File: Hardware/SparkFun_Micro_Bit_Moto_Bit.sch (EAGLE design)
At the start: 47 parts, among them J1 POWER_JACKPTH_LOCK, J2 CORTEX_DEBUGPTH, U1 CY8C4245LQI-483, U2 TPS62172, U3 micro:bit, U4 DRV8835

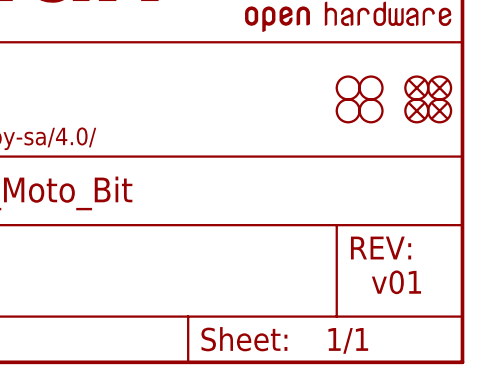
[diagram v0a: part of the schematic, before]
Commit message: V10 Changes
- Replaced 2x3 female headers to male
- Changed net label on heatsink mounting hole to GND
- Increased distance between exposed pad and motor connectors
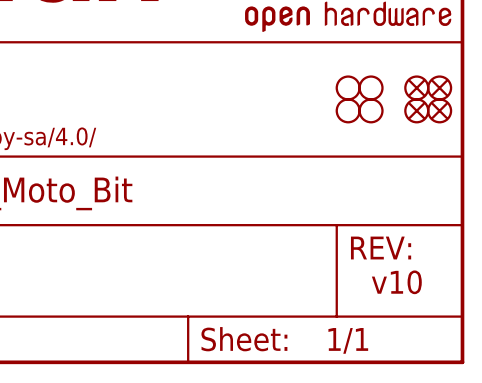
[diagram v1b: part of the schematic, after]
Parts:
- J6, J7, J8, J9: device SparkFun-Connectors:CONN_03X2FEMALE_SMD -> SparkFun-Connectors:CONN_03X2SMT
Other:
- note added: "v10"
- note removed: "v01"
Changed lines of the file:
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@@
 <parts>
 <part name="FRAME1" library="SparkFun-Aesthetics" deviceset="FRAME-LETTER" device=""/>
-<part name="J6" library="SparkFun-Connectors" deviceset="CONN_03X2" device="FEMALE_SMD"/>
-<part name="J7" library="SparkFun-Connectors" deviceset="CONN_03X2" device="FEMALE_SMD"/>
-<part name="J8" library="SparkFun-Connectors" deviceset="CONN_03X2" device="FEMALE_SMD"/>
+<part name="J6" library="SparkFun-Connectors" deviceset="CONN_03X2" device="SMT"/>
+<part name="J7" library="SparkFun-Connectors" deviceset="CONN_03X2" device="SMT"/>
+<part name="J8" library="SparkFun-Connectors" deviceset="CONN_03X2" device="SMT"/>
 <part name="J3" library="SparkFun-Connectors" deviceset="CONN_04" device="SMD_STRAIGHT_COMBO"/>
 <part name="GND22" library="SparkFun-PowerSymbols" deviceset="GND" device=""/>
@@
 <part name="FD3" library="SparkFun-Aesthetics" deviceset="FIDUCIAL" device="UFIDUCIAL"/>
 <part name="FD4" library="SparkFun-Aesthetics" deviceset="FIDUCIAL" device="UFIDUCIAL"/>
-<part name="J9" library="SparkFun-Connectors" deviceset="CONN_03X2" device="FEMALE_SMD"/>
+<part name="J9" library="SparkFun-Connectors" deviceset="CONN_03X2" device="SMT"/>
 <part name="GND26" library="SparkFun-PowerSymbols" deviceset="GND" device=""/>
 <part name="GND30" library="SparkFun-PowerSymbols" deviceset="GND" device=""/>
@@
 <text x="114.3" y="180.34" size="2.54" layer="97">micro:bit</text>
 <text x="166.37" y="11.43" size="2.54" layer="94">Alex Wende</text>
-<text x="238.76" y="7.62" size="2.54" layer="94">v01</text>
+<text x="238.76" y="7.62" size="2.54" layer="94">v10</text>
 <text x="2.54" y="142.24" size="2.54" layer="97">PSoC</text>
 <wire x1="111.76" y1="55.88" x2="111.76" y2="104.14" width="0.2032" layer="97" style="longdash"/>

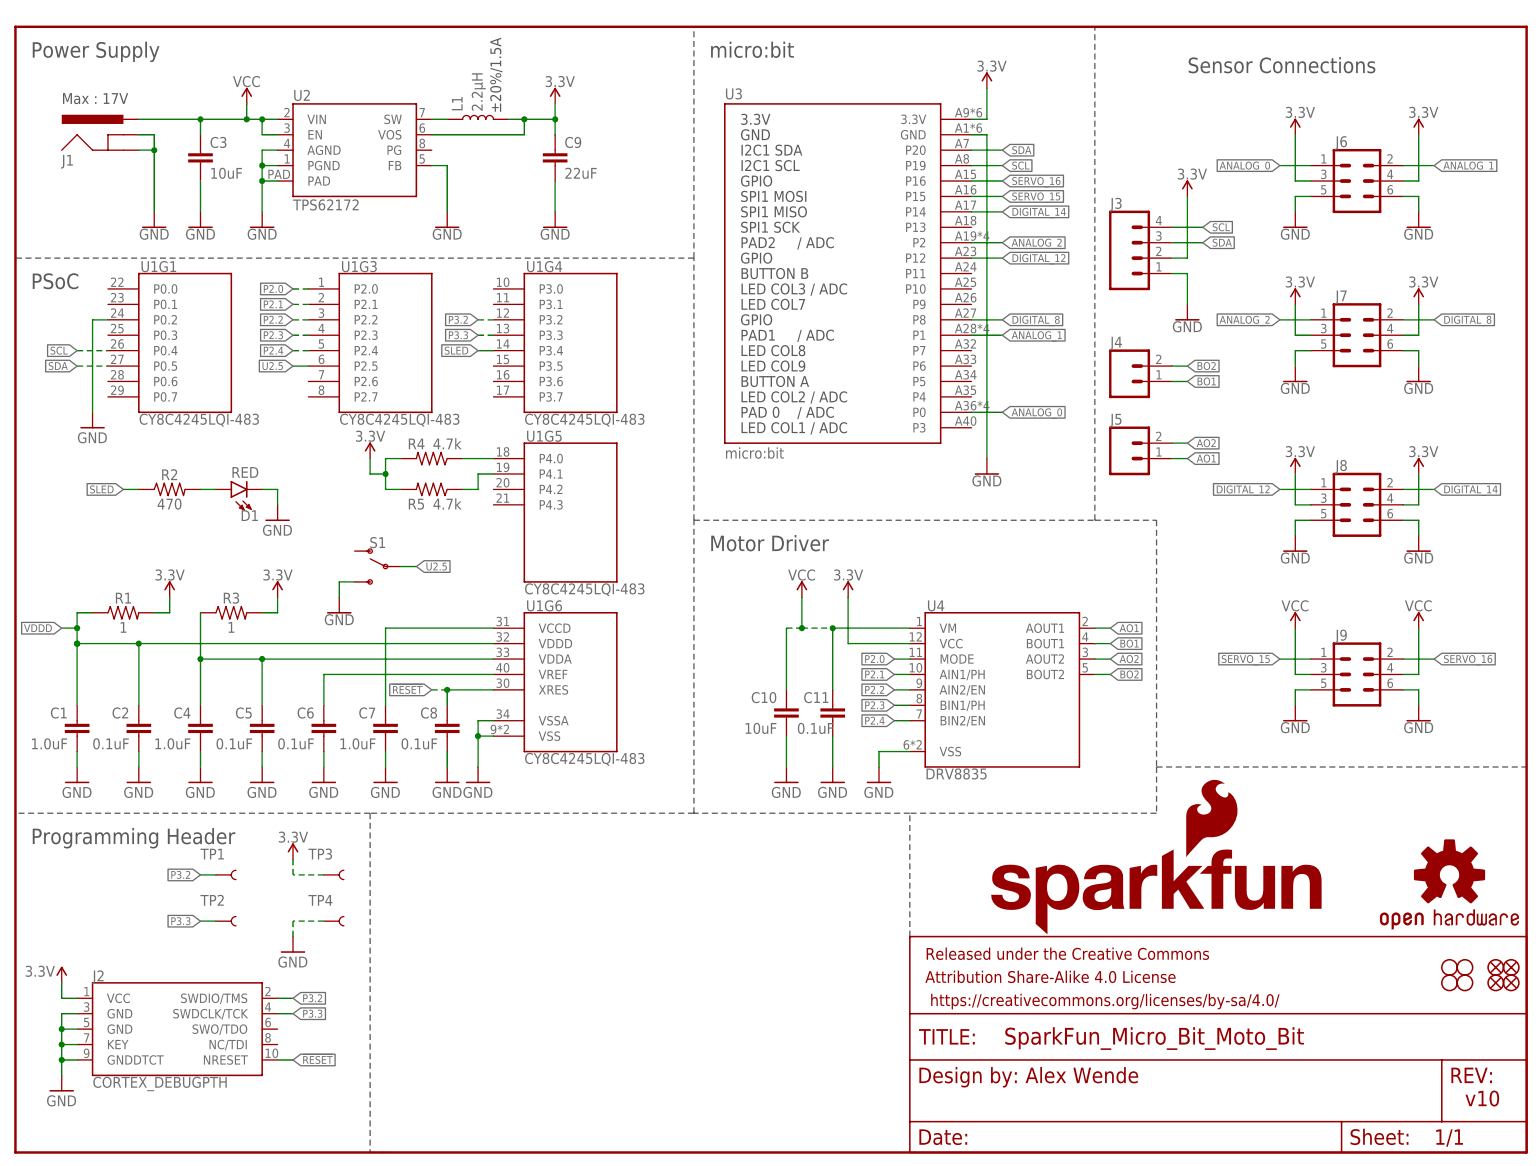
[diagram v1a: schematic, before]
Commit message: v20
-Updated silk to buzzard text
-Updated the supply range to 11V max
-Replaced 2.2uH inductor of buck regulator
-Added QWIIC Connector
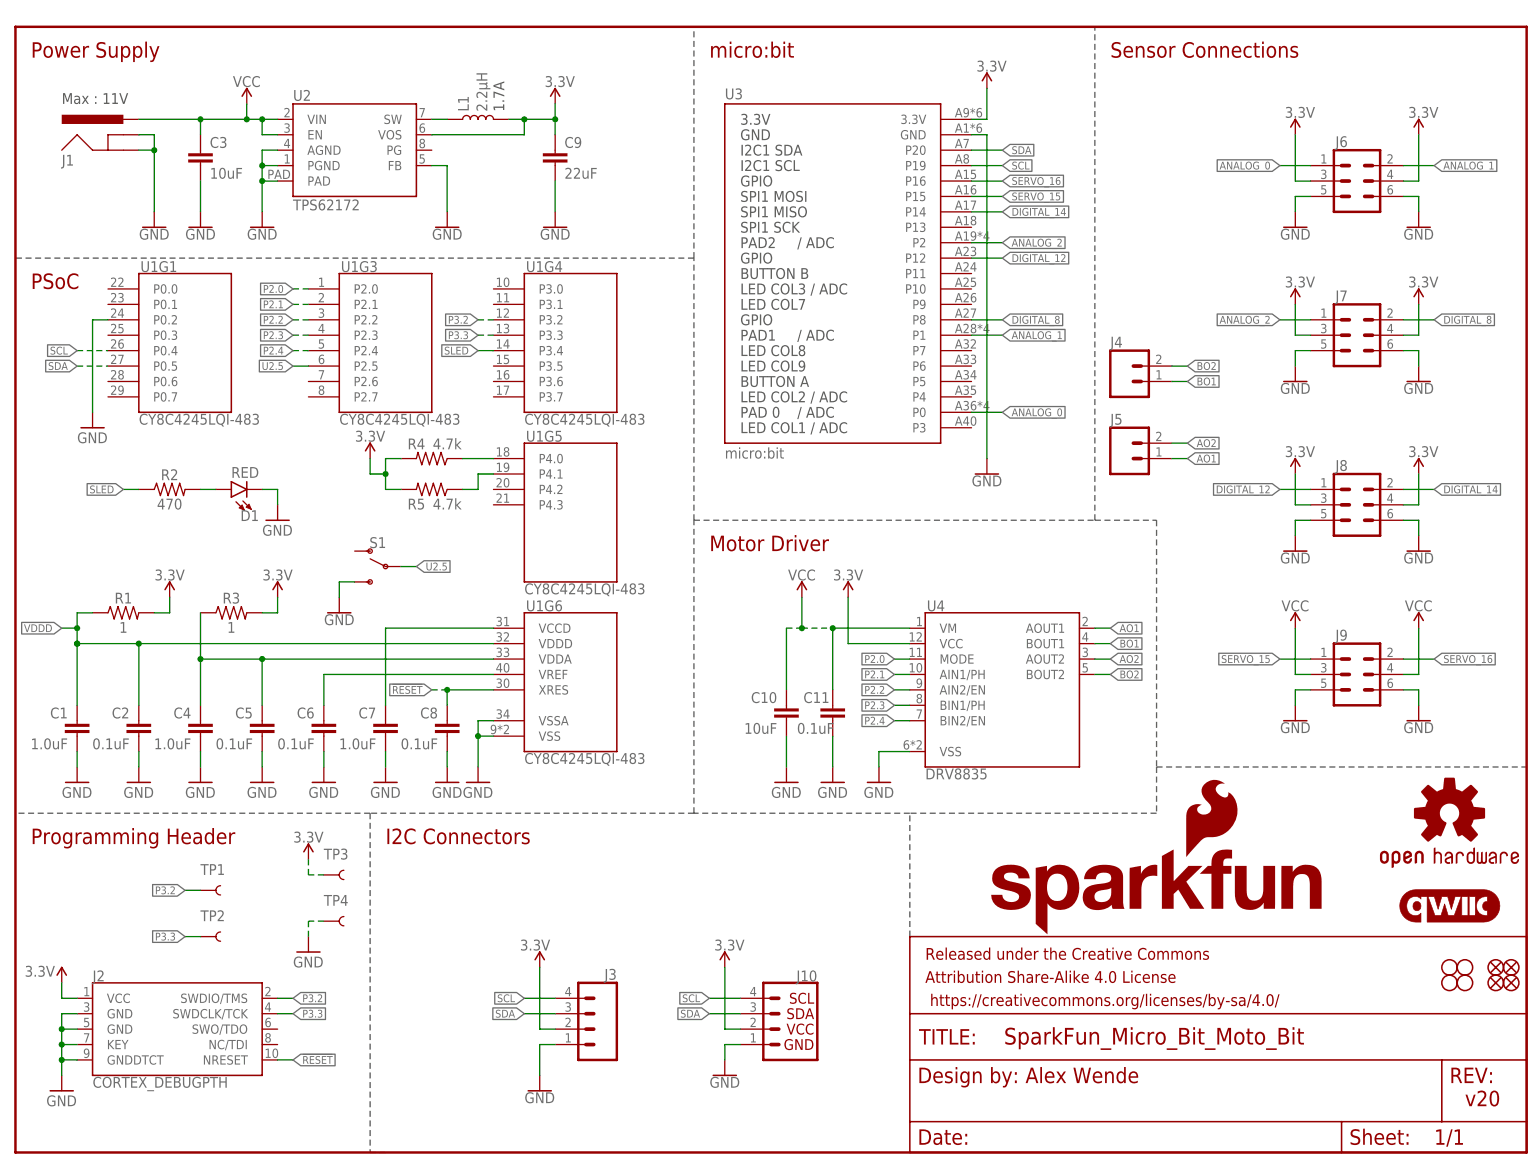
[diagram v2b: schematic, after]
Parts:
- added J10: (no value), SparkFun-Connectors:QWIIC_CONNECTOR
- added LOGO3: QWIIC_LOGO_5MM, SparkFun-Aesthetics:QWIIC_LOGO_5MM
- L1: value 2.2µH -> 2.2μH; device SparkFun-Coils:INDUCTOR-VLF4012AT-2.2UH -> SparkFun-Coils:2.2μH-0805_WIDE-2.2μH-1.7A-0.14OHM
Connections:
- net 3.3V: now also J10.2
- net GND: now also J10.1
- net SCL: now also J10.4
- net SDA: now also J10.3
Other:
- note added: "1.7A"
- note added: "I2C Connectors"
- note added: "Max : 11V"
- note added: "v20"
- note removed: "Max : 17V"
- note removed: "v10"
- note removed: "±20%/1.5A"
- moved on the sheet: J3, TP1, TP2

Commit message: QC Fixes
Replaced switch with short leads
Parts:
- S1: device SparkFun-Switches:SWITCH-SPDT-PTH-11.6X4.0MM -> SparkFun-Switches:SWITCH-SPDT-PTH-11.6X4.0MM-SHORT_LEADS
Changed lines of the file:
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@@
 <part name="SUPPLY3" library="SparkFun-PowerSymbols" deviceset="VCC" device=""/>
 <part name="SUPPLY8" library="SparkFun-PowerSymbols" deviceset="VCC" device=""/>
-<part name="S1" library="SparkFun-Switches" deviceset="SWITCH-SPDT" device="-PTH-11.6X4.0MM"/>
+<part name="S1" library="SparkFun-Switches" deviceset="SWITCH-SPDT" device="-PTH-11.6X4.0MM-SHORT_LEADS"/>
 <part name="GND31" library="SparkFun-Aesthetics" deviceset="GND" device=""/>
 <part name="SUPPLY15" library="SparkFun-PowerSymbols" deviceset="VCC" device=""/>

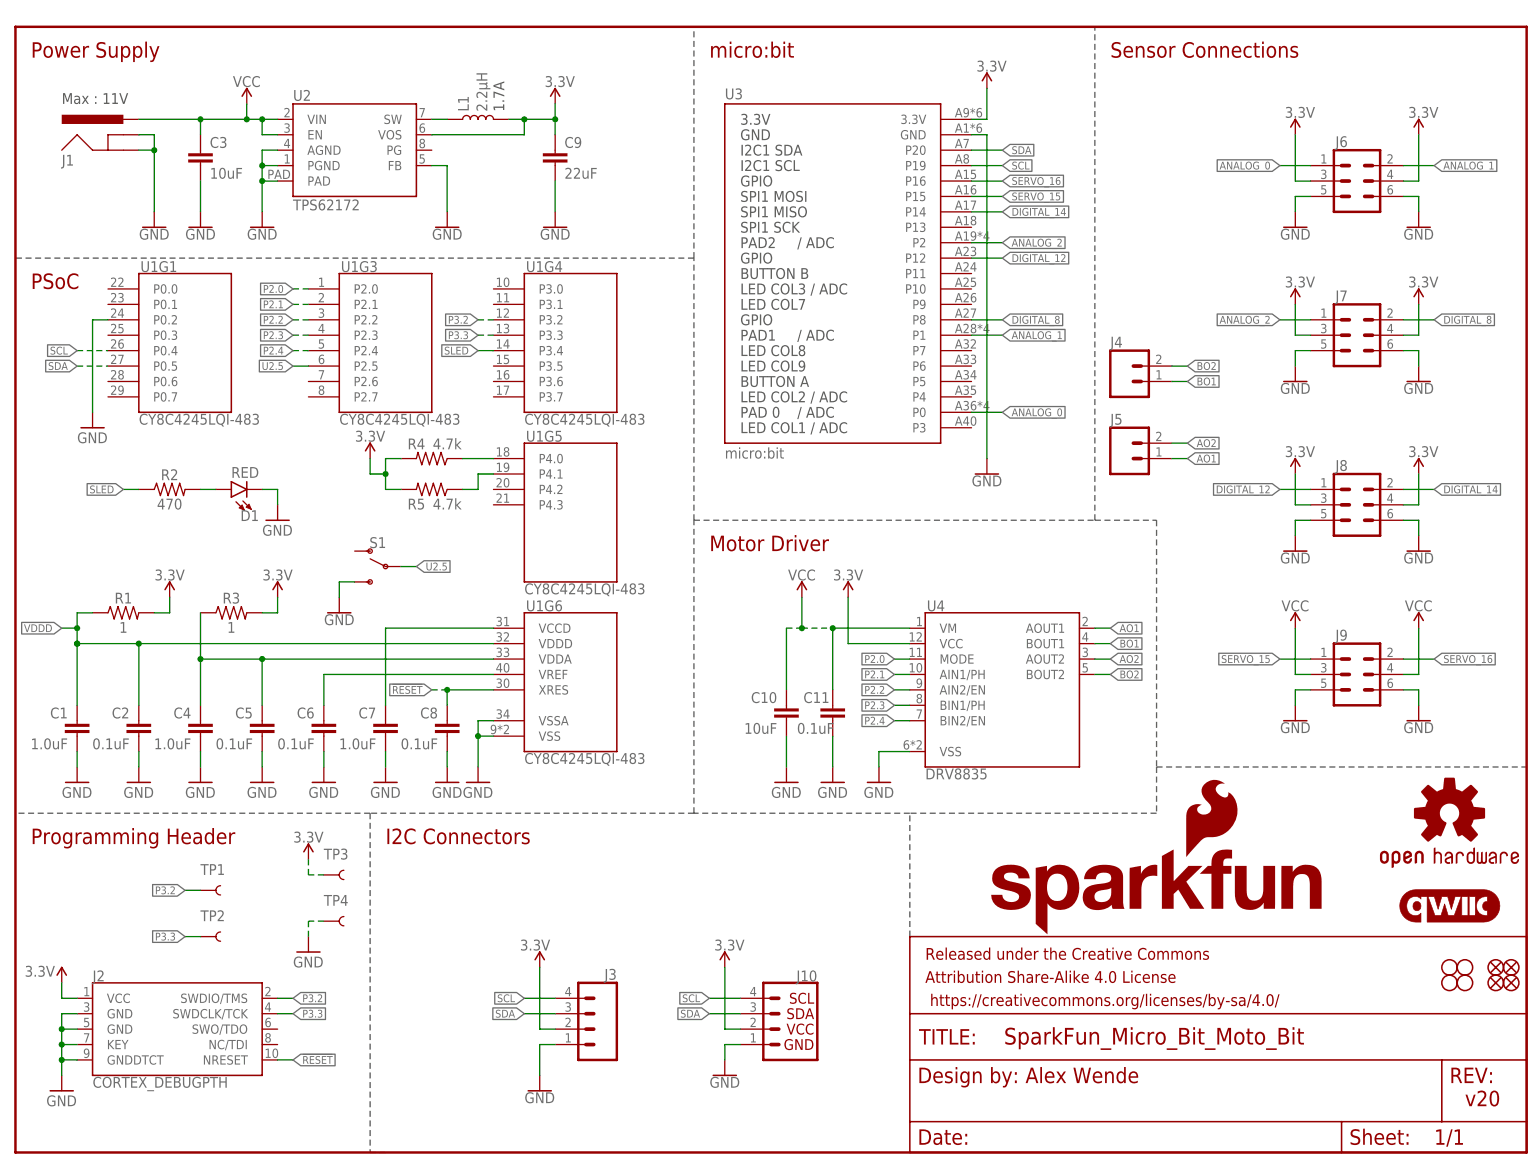
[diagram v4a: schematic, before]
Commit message: v20_cont
Added micro:bit SMD footprint and test points.
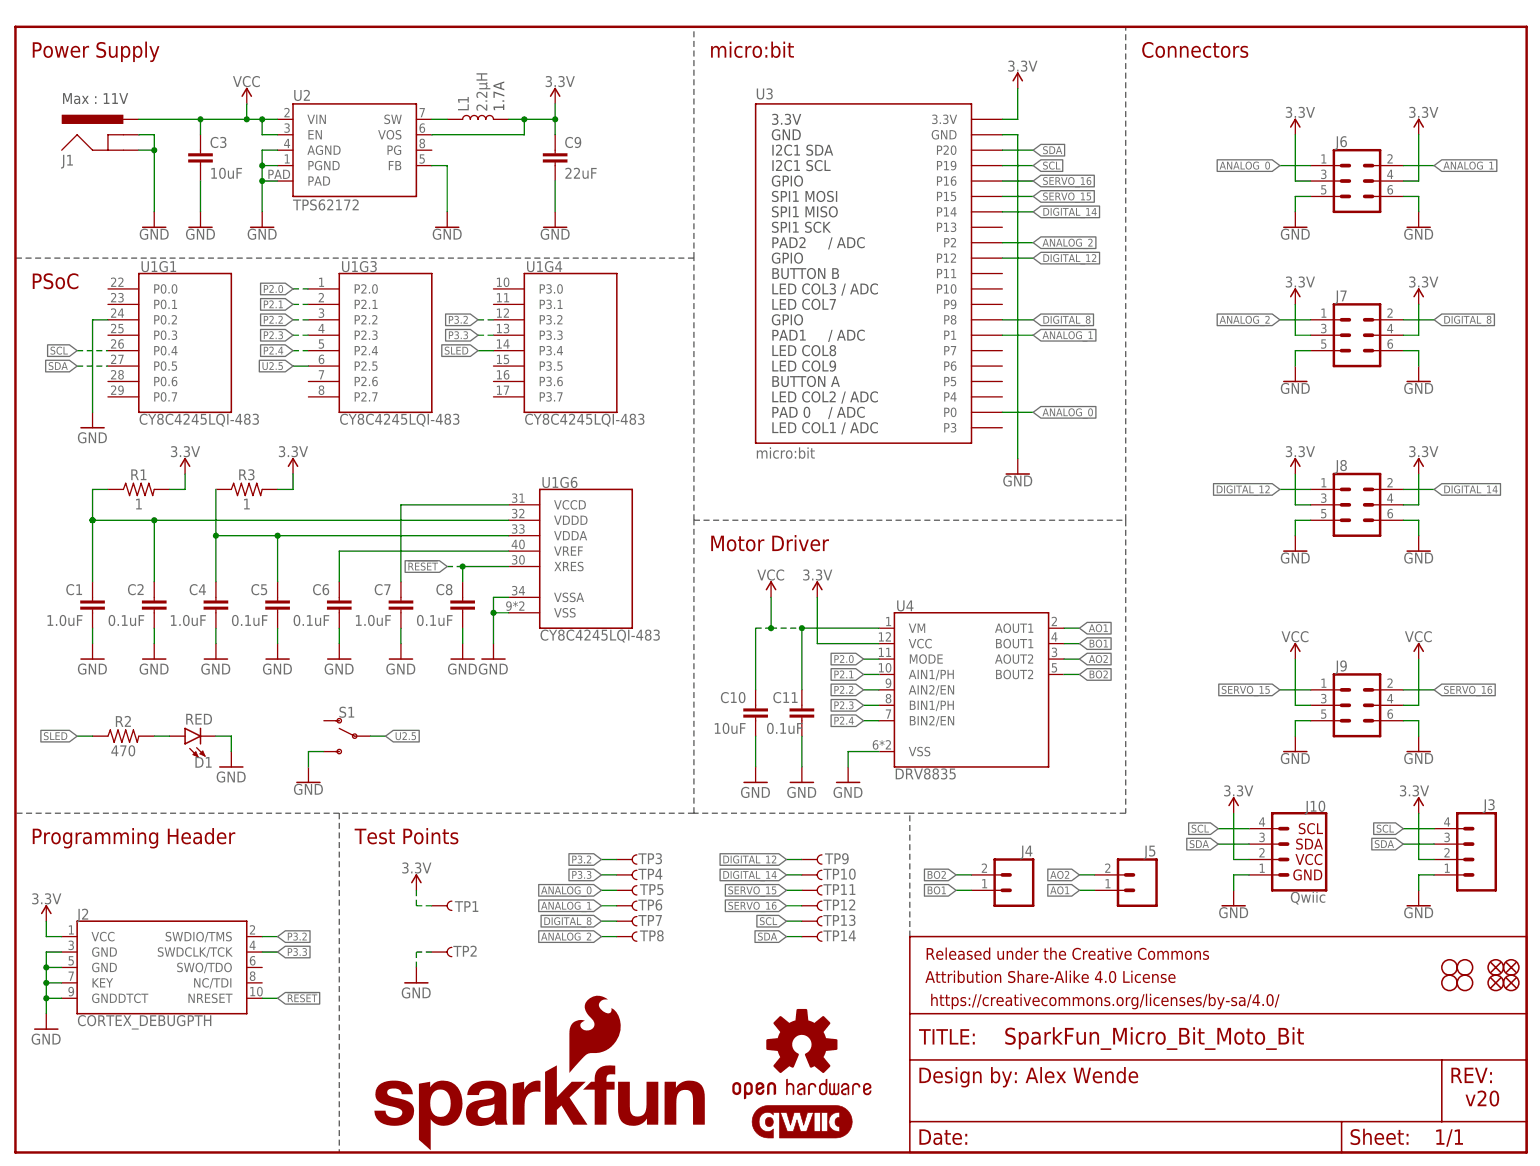
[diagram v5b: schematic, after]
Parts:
- removed R4, R5: 4.7k, SparkFun-Resistors:4.7KOHM-0603-1/10W-1%
- added TP10, TP11, TP12, TP13, TP14, TP5, TP6, TP7, TP8, TP9: TEST-POINTTP_15TH_THRU, SparkFun-Connectors:TEST-POINTTP_15TH_THRU
- J10: value (none) -> Qwiic
- U3: device Micro_Bit_Parts:MICRO:BITLEDS_UP -> SparkFun-Connectors:MICRO:BIT_RA
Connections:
- removed net N$6: R4.1, U1G5.P4.0
- removed net N$7: R5.1, U1G5.P4.1
- net 3.3V: now also TP1.1; no longer R4.2, R5.2, TP3.1
- net ANALOG_0: now also TP5.1
- net ANALOG_1: now also TP6.1
- net ANALOG_2: now also TP8.1
- net DIGITAL_12: now also TP9.1
- net DIGITAL_14: now also TP10.1
- net DIGITAL_8: now also TP7.1
- net GND: now also TP2.1; no longer TP4.1
- net P3.2: now also TP3.1; no longer TP1.1
- net P3.3: now also TP4.1; no longer TP2.1
- net SCL: now also TP13.1
- net SDA: now also TP14.1
- net SERVO_15: now also TP11.1
- net SERVO_16: now also TP12.1
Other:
- note added: "Connectors"
- note added: "Test Points"
- note removed: "I2C Connectors"
- note removed: "Sensor Connections"
- moved on the sheet: C1, C10, C11, C2, C4, C5, C6, C7, C8, D1, J10, J2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
